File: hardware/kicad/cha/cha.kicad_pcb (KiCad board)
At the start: 4 copper layers, 173 x 134 mm, 137 parts, among them J1 AES_CHA, J2 CONF C, J3 CONF SM, J4 microSD, J5 Câble PROG-CHA, SW1 Retour menu, U1 AMS1117-3.3, U10 74AHCT1G32, U11 74LVC1G07, U12 iCE40HX4K-TQ144, U13 AS4C32M16SB-6TIN, U14 iCE40HX4K-TQ144, U15 IS61WV10248EDBLL-10TLI, U2 AP2112K-1.2, U3 74LVC16244A, U4 74LVC16244A, U5 74LVC16244A, U6 74LVC16244A, U7 74AHCT16244, U8 74AHCT16244, U9 74AHCT244, X1 25 MHz 3,3 V, X2 25 MHz 3,3 V

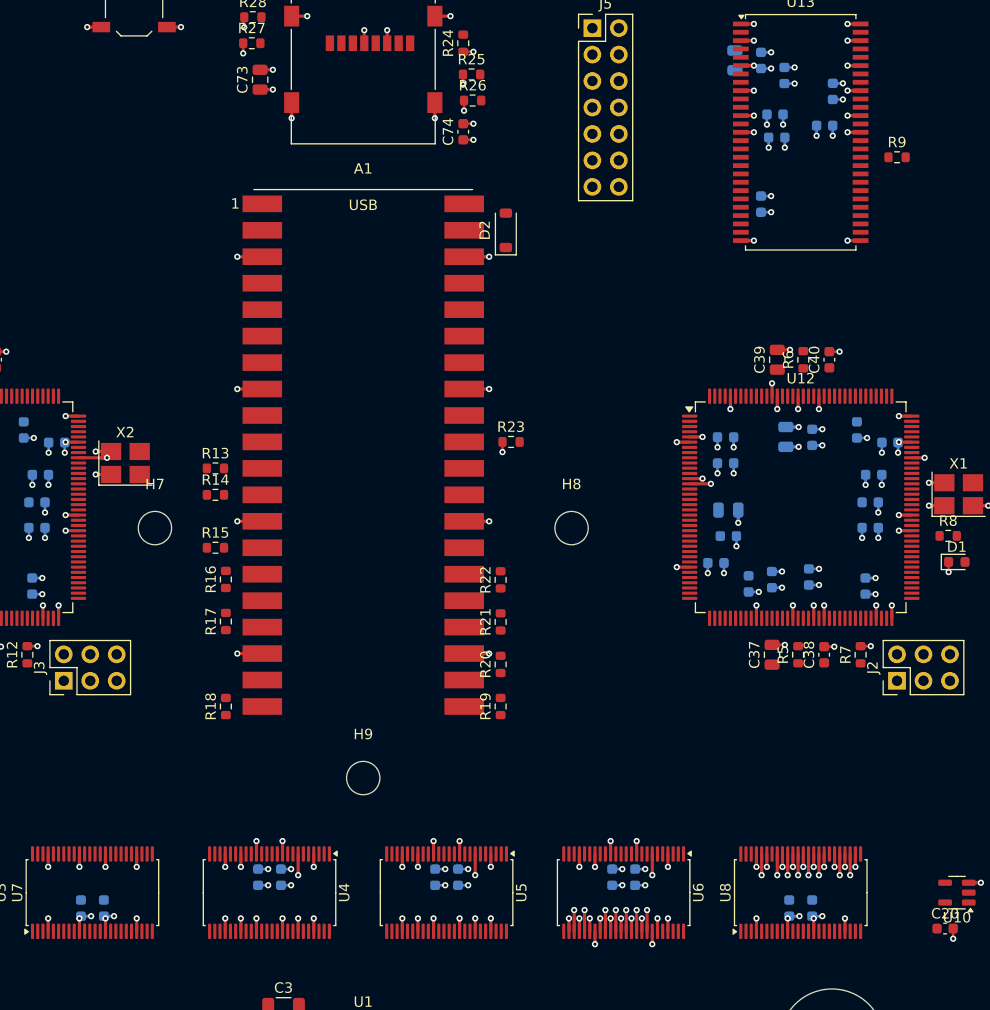
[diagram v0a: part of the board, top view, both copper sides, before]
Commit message: PCB : vias vers les plans écartés de toutes les pastilles CMS
Freerouting refuse un via sur une pastille, même de son réseau.

Co-Authored-By: Claude Opus 5.5 <noreply@anthropic.com>
Claude-Session: https://claude.ai/code/session_01WKfXP1YJ8otGxZ5dsY6Agh
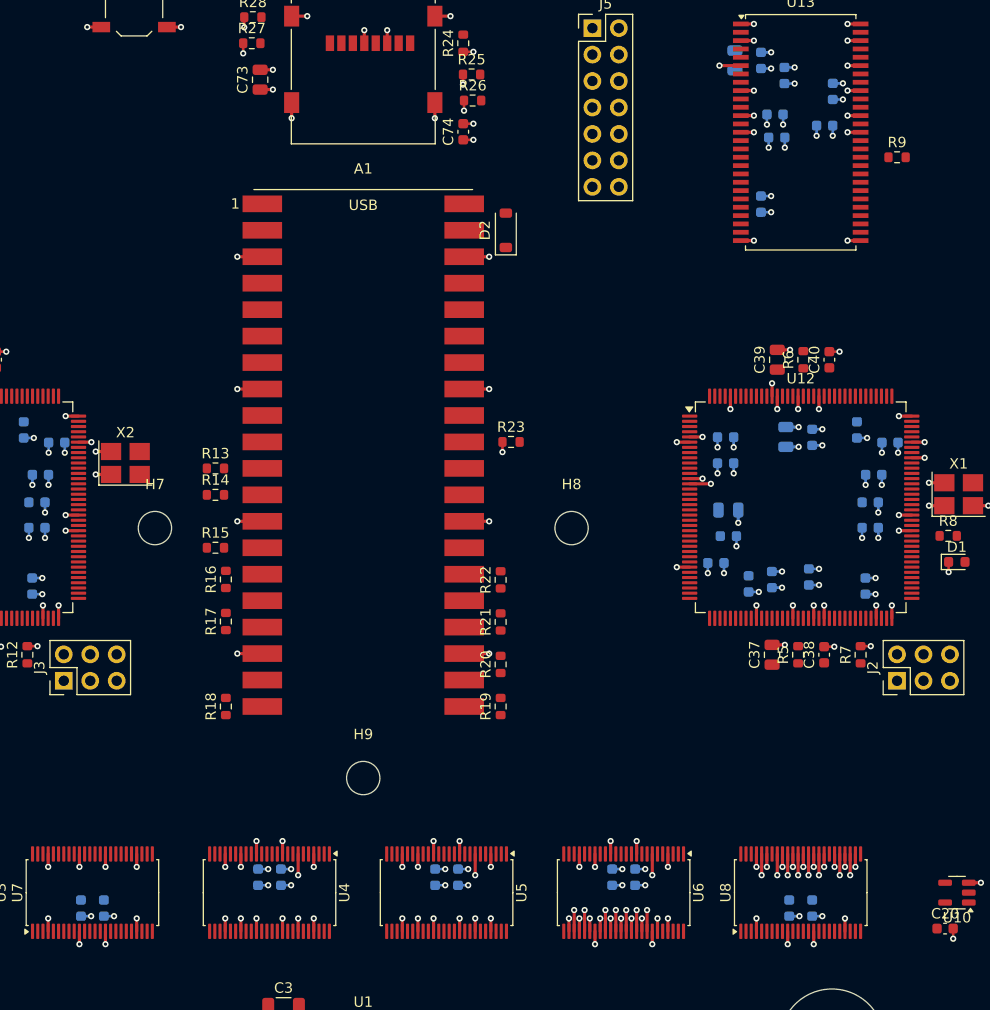
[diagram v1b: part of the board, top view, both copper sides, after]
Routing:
- net +3V3: track 128.2 -> 125.5 mm, vias 108 -> 107
- net GND: track 308.0 -> 308.8 mm

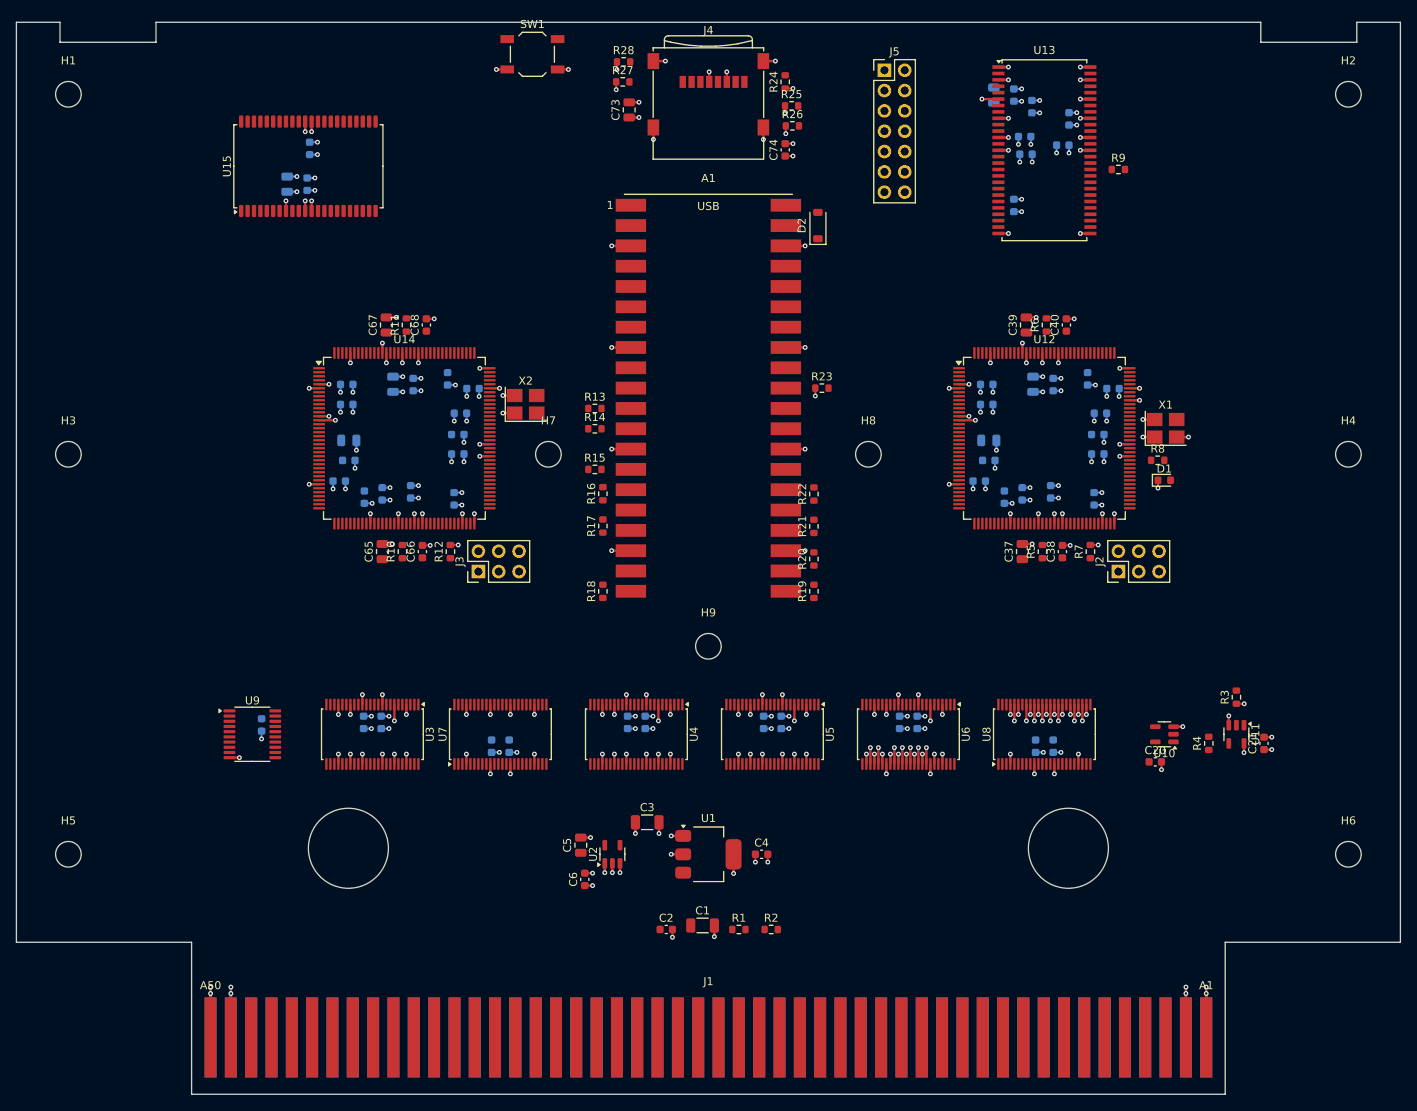
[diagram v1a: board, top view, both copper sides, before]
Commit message: Carte CHA routée (4 couches) : 6 signaux et 2 raccordements restants
Routage Freerouting en 12 passes, raccordements aux plans complétés
après routage. DRC KiCad : aucune violation d'isolement ni
court-circuit ; restent 6 lignes du bus P côté droit du FPGA SM (U14)
et 2 raccordements aux plans (X2.2, U14.100), dans le couloir étroit
entre le FPGA SM, son oscillateur et l'entretoise H7.

Co-Authored-By: Claude Opus 5.5 <noreply@anthropic.com>
Claude-Session: https://claude.ai/code/session_01WKfXP1YJ8otGxZ5dsY6Agh
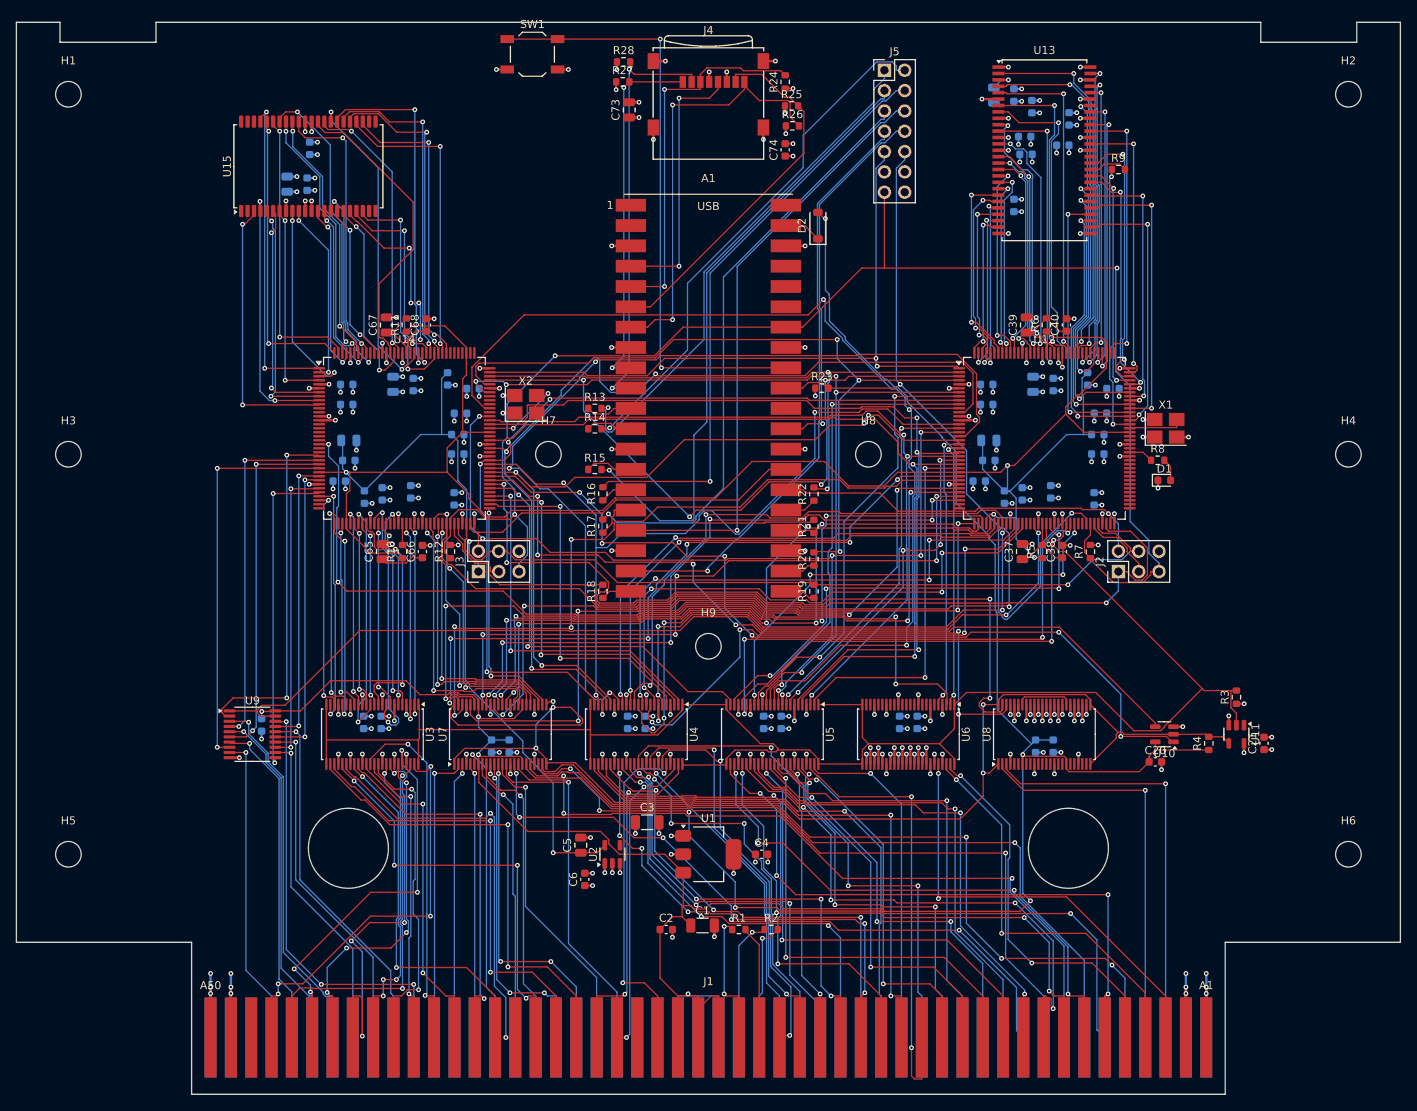
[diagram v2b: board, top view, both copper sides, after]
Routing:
- net +5V: track 0.00 -> 333.5 mm, vias 0 -> 7
- net +1V2: track 0.00 -> 318.6 mm, vias 0 -> 5
- net XLAT_EN_N: track 0.00 -> 213.9 mm
- net CDONE: track 0.00 -> 189.3 mm, vias 0 -> 3
- net CRESET_N: track 0.00 -> 186.4 mm, vias 0 -> 3
- net OE5_N: track 0.00 -> 157.7 mm, vias 0 -> 5
- net P3: track 0.00 -> 130.3 mm, vias 0 -> 3
- net SDD_OE5_N: track 0.00 -> 129.8 mm
- net P12: track 0.00 -> 117.8 mm, vias 0 -> 3
- net P14: track 0.00 -> 117.7 mm, vias 0 -> 3
- net P5: track 0.00 -> 115.7 mm, vias 0 -> 6
- net CHA_SCK: track 0.00 -> 109.9 mm, vias 0 -> 2
- net P6: track 0.00 -> 109.4 mm, vias 0 -> 3
- net P0: track 0.00 -> 109.4 mm, vias 0 -> 5
- net PCK2B: track 0.00 -> 108.8 mm, vias 0 -> 4
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
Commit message: PCB : entretoises H7 et H8 remontées à y = 75 mm
En (130, 100) et (170, 100), elles bouchaient le couloir de sortie du
côté droit du FPGA V / SM (6 lignes du bus P et 2 raccordements non
routés sur la carte CHA). Cartes régénérées, contrôle Freerouting sans
violation ; nouveau routage en cours.

Co-Authored-By: Claude Opus 5.5 <noreply@anthropic.com>
Claude-Session: https://claude.ai/code/session_01WKfXP1YJ8otGxZ5dsY6Agh
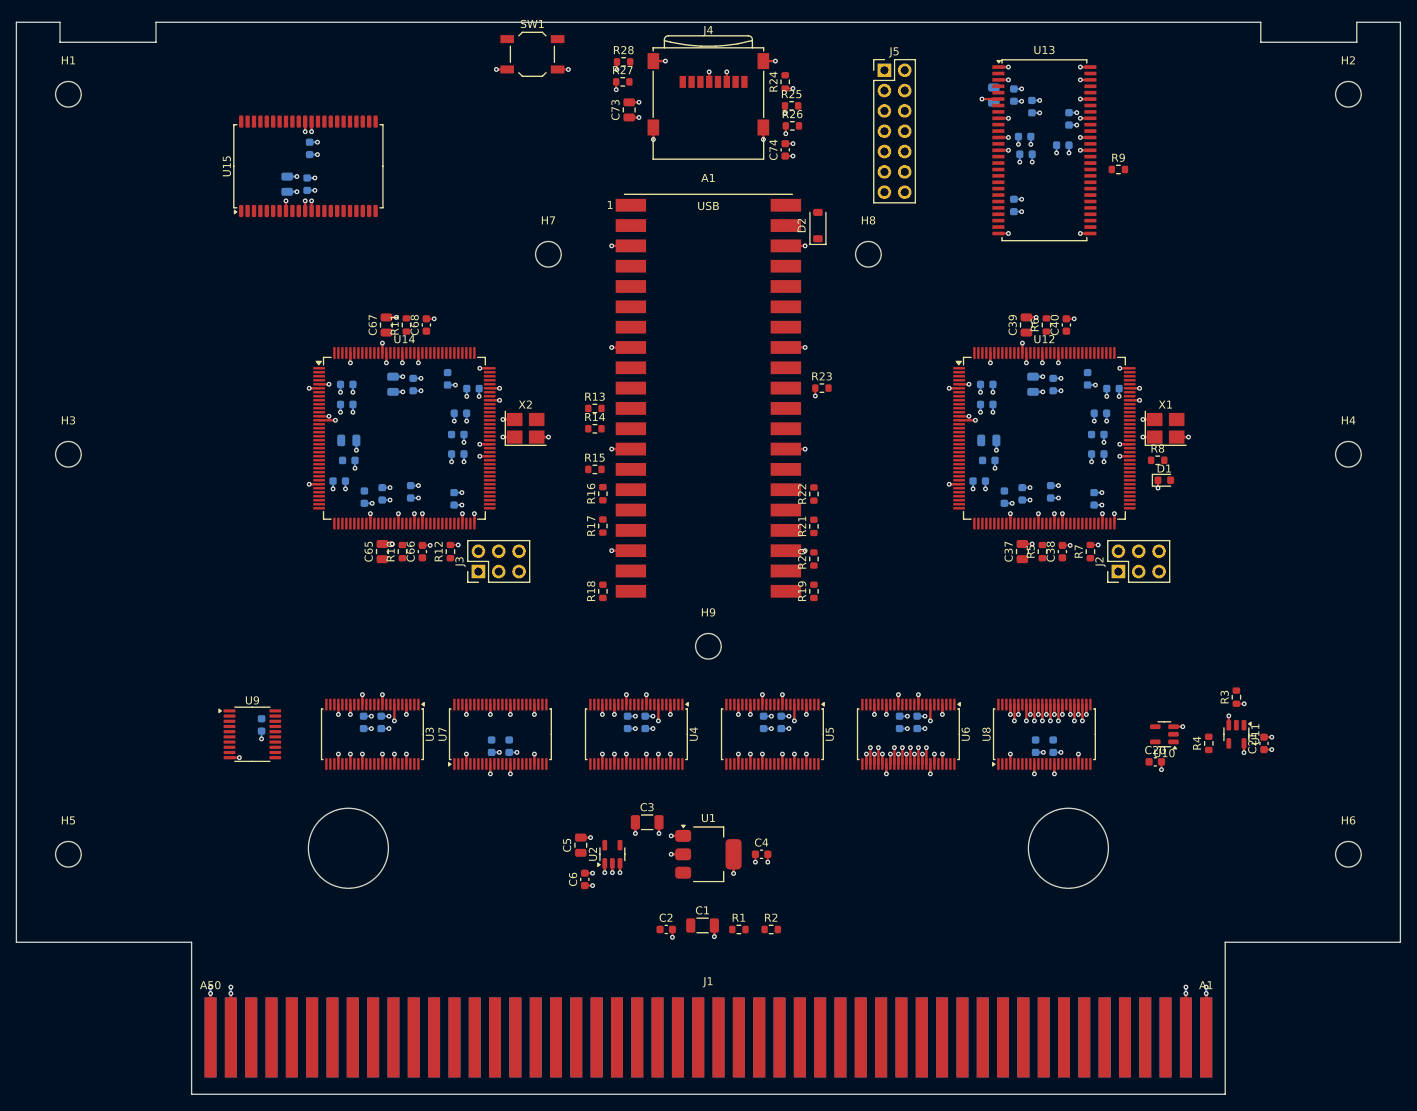
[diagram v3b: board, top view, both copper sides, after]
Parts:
- moved H7 25.0 mm to (130.0, 75.0)
- moved H8 25.0 mm to (170.0, 75.0)
- moved X2 3.00 mm to (127.2, 96.8)
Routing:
- net +5V: track 333.5 -> 0.00 mm, vias 7 -> 0
- net +1V2: track 318.6 -> 0.00 mm, vias 5 -> 0
- net XLAT_EN_N: track 213.9 -> 0.00 mm
- net CDONE: track 189.3 -> 0.00 mm, vias 3 -> 0
- net CRESET_N: track 186.4 -> 0.00 mm, vias 3 -> 0
- net OE5_N: track 157.7 -> 0.00 mm, vias 5 -> 0
- net P3: track 130.3 -> 0.00 mm, vias 3 -> 0
- net SDD_OE5_N: track 129.8 -> 0.00 mm
- net P12: track 117.8 -> 0.00 mm, vias 3 -> 0
- net P14: track 117.7 -> 0.00 mm, vias 3 -> 0
- net P5: track 115.7 -> 0.00 mm, vias 6 -> 0
- net CHA_SCK: track 109.9 -> 0.00 mm, vias 2 -> 0
- net P6: track 109.4 -> 0.00 mm, vias 3 -> 0
- net P0: track 109.4 -> 0.00 mm, vias 5 -> 0
- net PCK2B: track 108.8 -> 0.00 mm, vias 4 -> 0
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
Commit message: Carte CHA routée : 3 liaisons restantes (DOTA, GAD0, P4)
Après le déplacement des entretoises H7/H8 : raccordements aux plans
complets ; restent DOTA et GAD0 (FPGA C -> 74AHCT16244 U7) et une
broche P4 du FPGA SM. DRC : aucune violation d'isolement ni
court-circuit. route.py --continue : reprise d'un routage existant.

Co-Authored-By: Claude Opus 5.5 <noreply@anthropic.com>
Claude-Session: https://claude.ai/code/session_01WKfXP1YJ8otGxZ5dsY6Agh
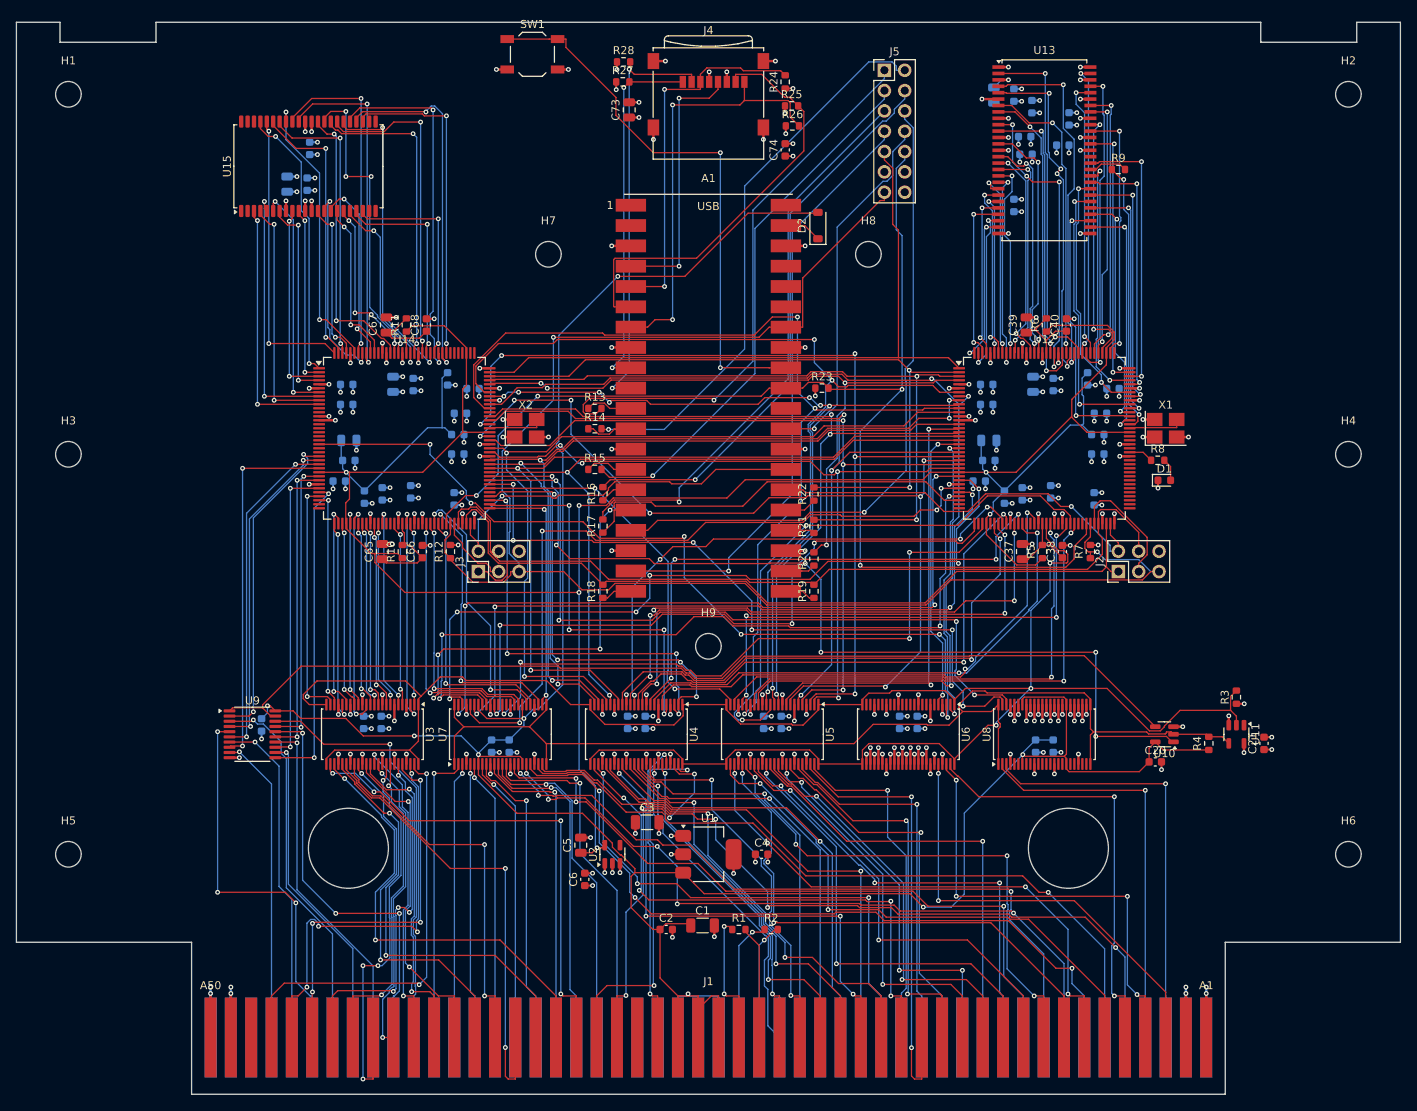
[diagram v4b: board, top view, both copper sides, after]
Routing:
- net +5V: track 0.00 -> 348.7 mm, vias 0 -> 8
- net +1V2: track 0.00 -> 304.2 mm, vias 0 -> 6
- net XLAT_EN_N: track 0.00 -> 254.0 mm, vias 0 -> 3
- net CRESET_N: track 0.00 -> 200.4 mm, vias 0 -> 2
- net CDONE: track 0.00 -> 155.0 mm, vias 0 -> 4
- net OE5_N: track 0.00 -> 136.9 mm
- net P3: track 0.00 -> 128.9 mm, vias 0 -> 3
- net P1: track 0.00 -> 127.3 mm, vias 0 -> 3
- net SDD_OE5_N: track 0.00 -> 125.8 mm
- net P8: track 0.00 -> 117.2 mm, vias 0 -> 5
- net SDD_OE_N: track 0.00 -> 115.7 mm, vias 0 -> 6
- net P7: track 0.00 -> 115.5 mm, vias 0 -> 7
- net P0: track 0.00 -> 114.9 mm, vias 0 -> 3
- net CHA_IO0: track 0.00 -> 105.3 mm
- net PCK2B: track 0.00 -> 104.4 mm, vias 0 -> 6
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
